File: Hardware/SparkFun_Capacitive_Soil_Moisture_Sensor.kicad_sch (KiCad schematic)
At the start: 21 parts, among them J1 Qwiic_RA, J2 Qwiic_RA, U1 CAP1203

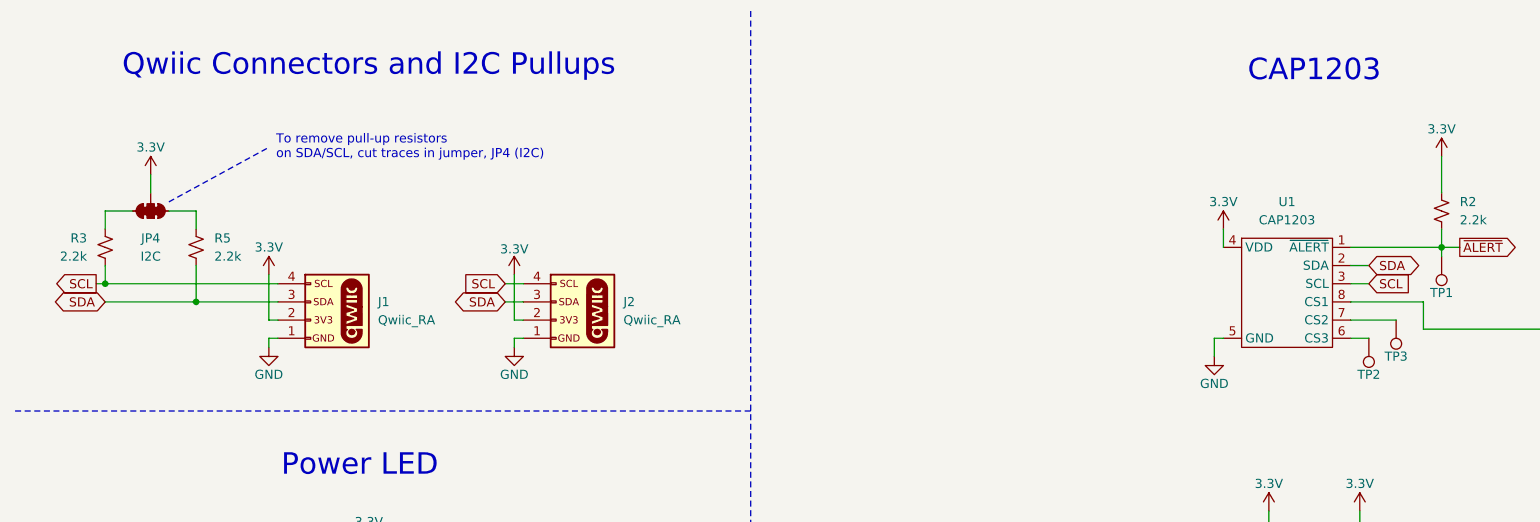
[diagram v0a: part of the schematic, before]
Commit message: Cleanup test points and silkscreen, remove acid traps
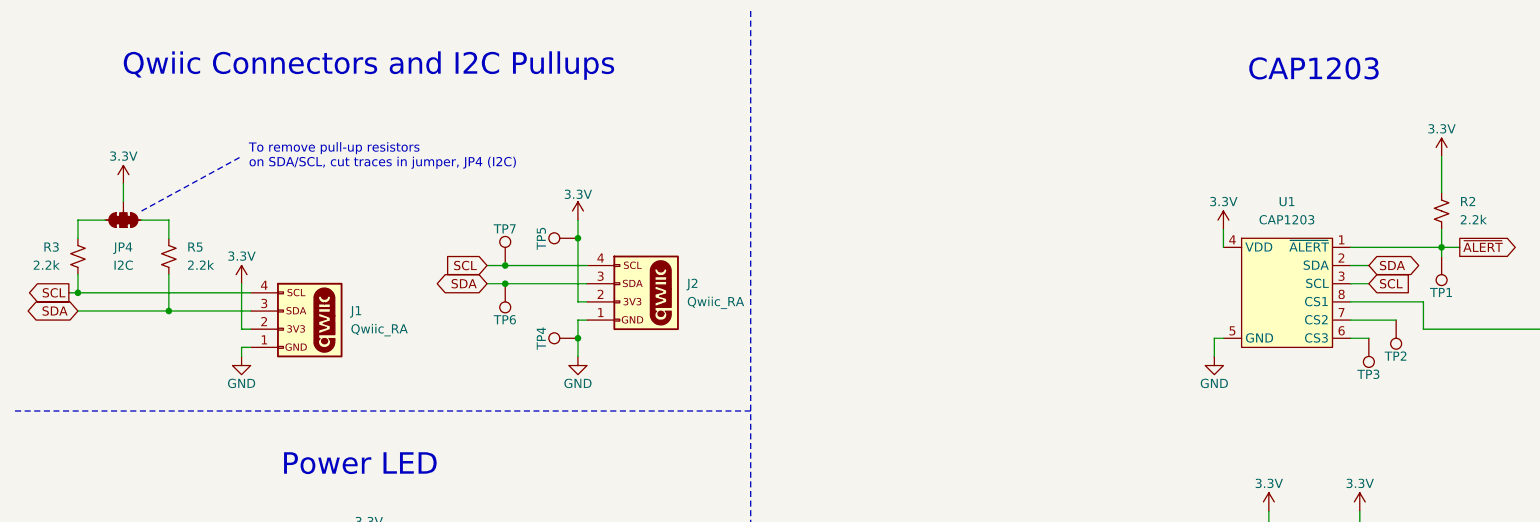
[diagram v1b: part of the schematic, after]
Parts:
- removed TP1, TP2, TP3: 1.25mm, SparkFun-Connector:TestPoint-1.25mm, symbol SparkFun-Connector:TestPoint_1.25mm
- added TP1, TP2, TP3, TP4, TP5, TP6, TP7: 1.0mm, SparkFun-Connector:TestPoint-1.0mm, symbol SparkFun-Connector:TestPoint_1.0mm
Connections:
- net 3.3V: now also TP5.1
- net GND: now also TP4.1
- net SCL: now also TP7.1
- net SDA: now also TP6.1
- net ~{ALERT}: now also TP1.1
- net at U1.7 (CS2): now also TP2.1
- net at U1.6 (CS3): now also TP3.1
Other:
- moved on the sheet: J1, J2, JP4, R3, R5

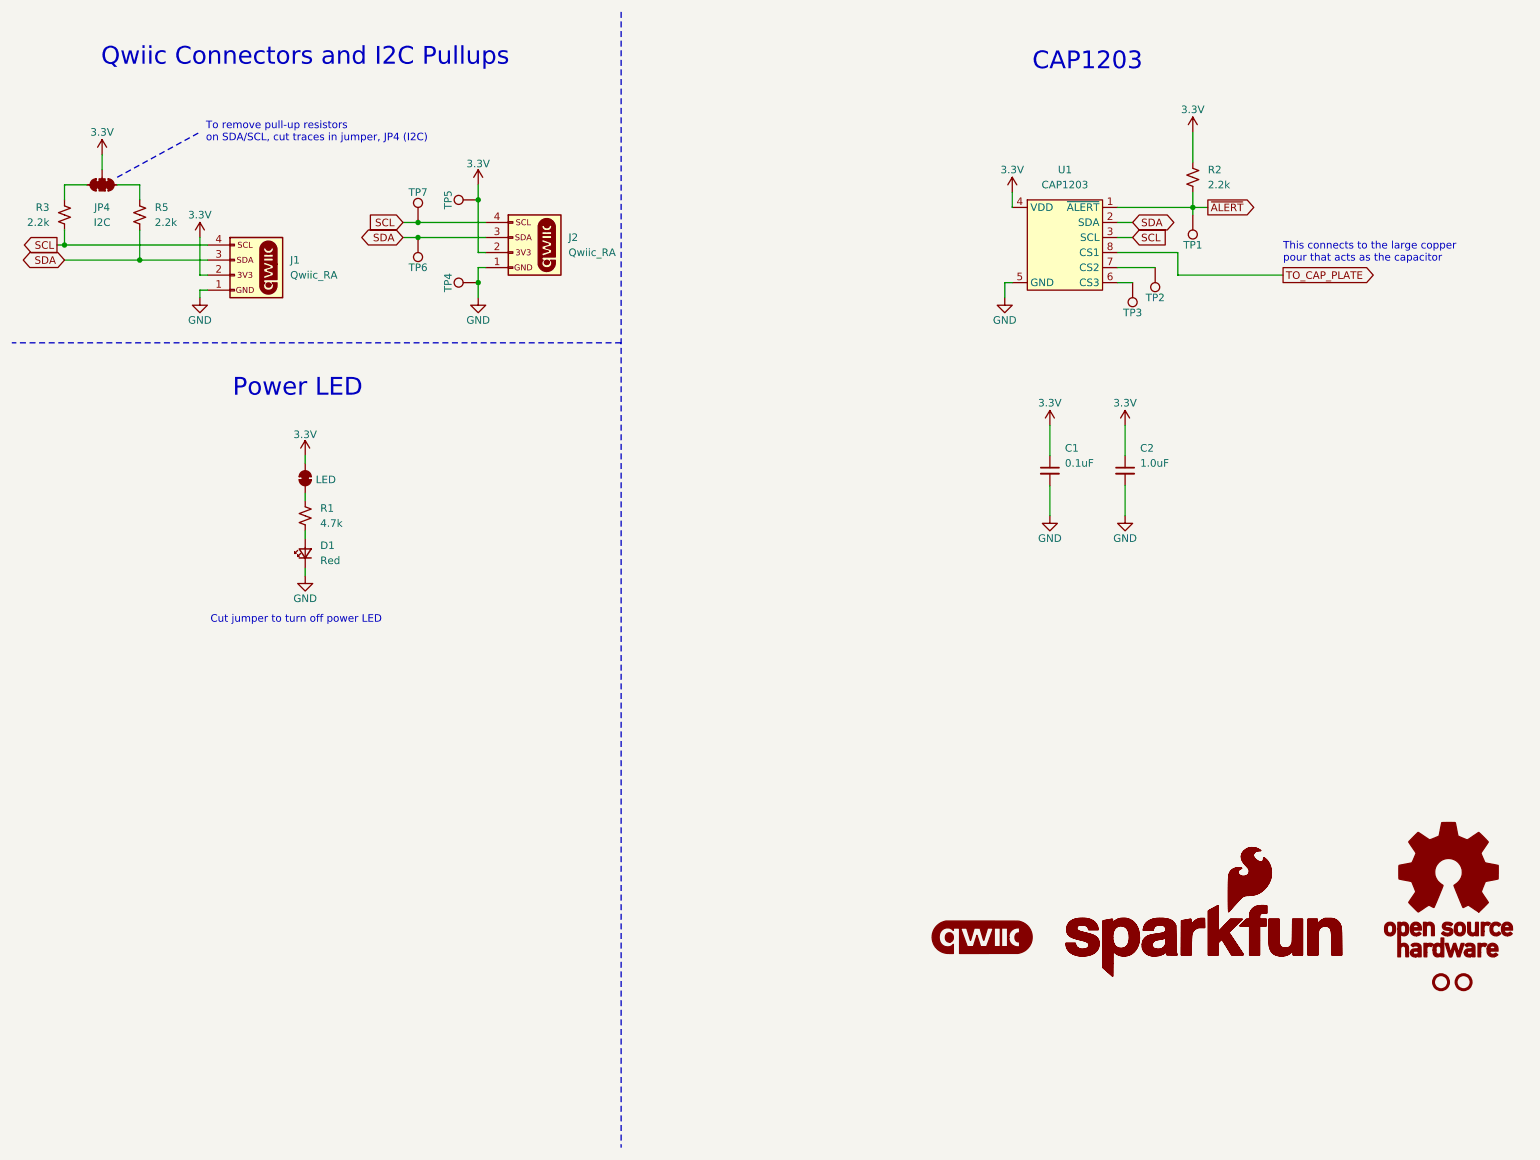
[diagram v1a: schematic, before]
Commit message: Make schematic updates from preliminary review
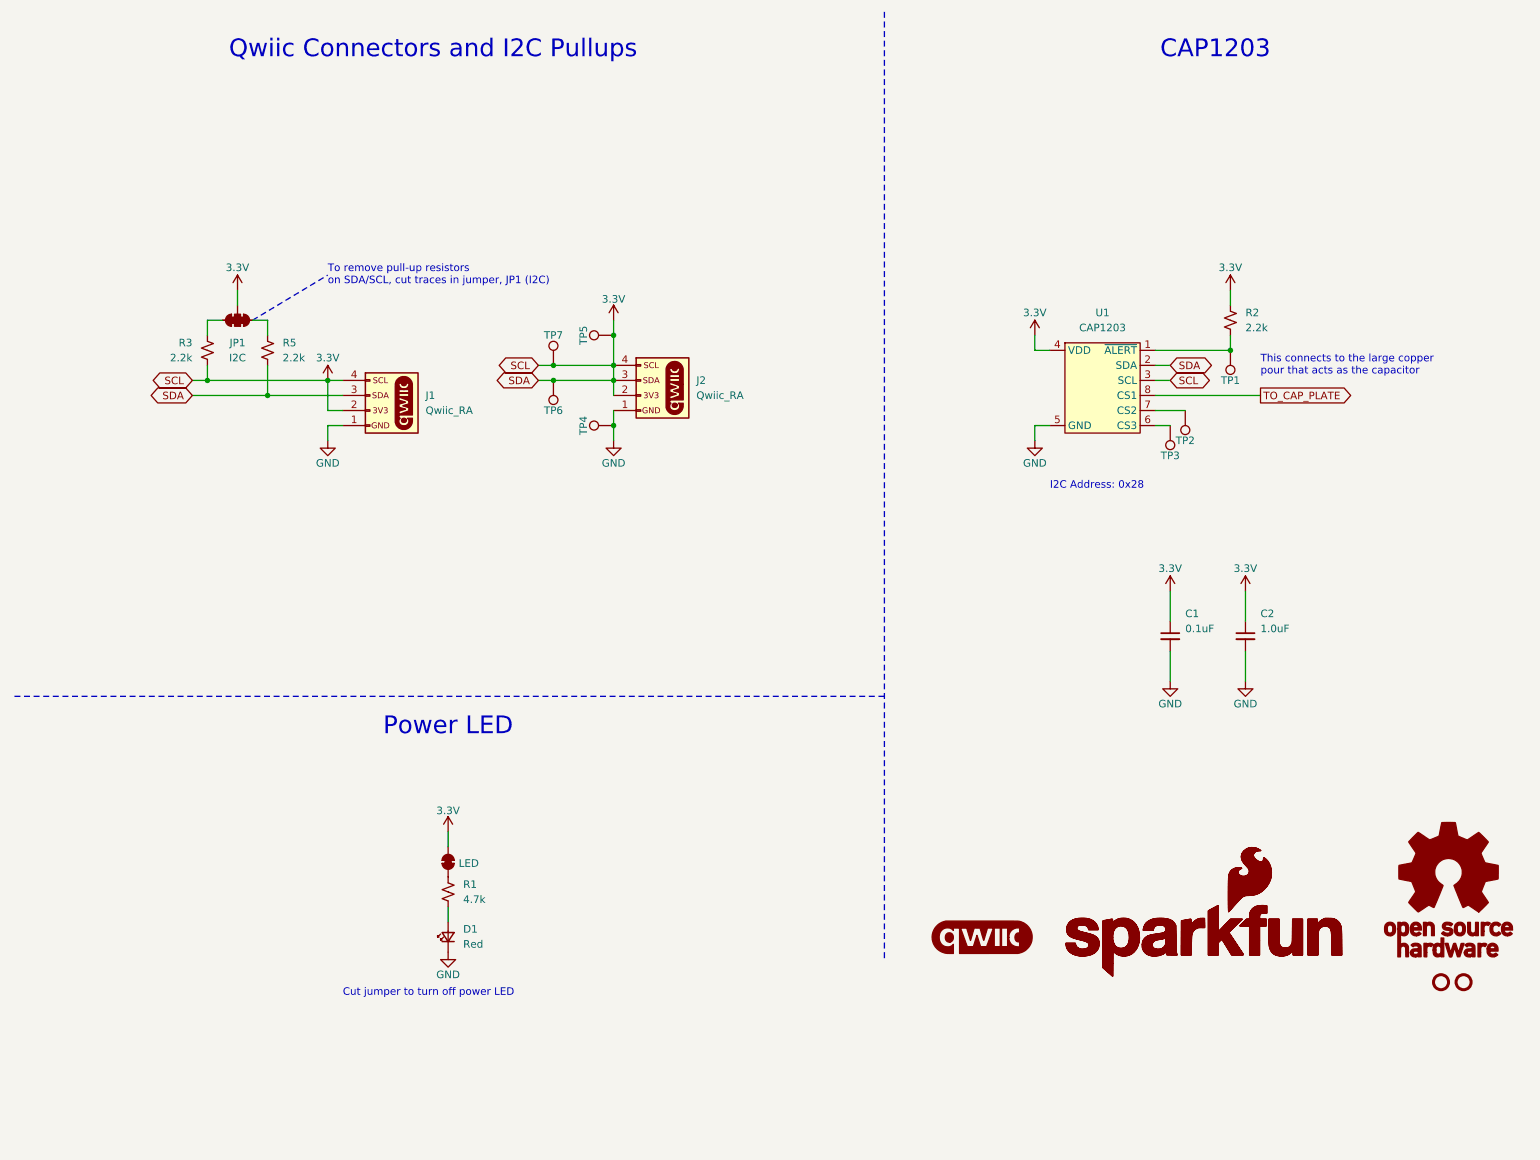
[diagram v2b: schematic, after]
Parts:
- renumbered JP4 to JP1
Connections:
- net SCL is gone; now on net 3.3V: J1.4 (Pin_4), J2.4 (Pin_4), R3.2, TP7.1, U1.3 (SCL)
- net SDA is gone; now on net 3.3V: J1.3 (Pin_3), J2.3 (Pin_3), R5.2, TP6.1, U1.2 (SDA)
- net ~{ALERT}: no longer names the net of R2.2, TP1.1, U1.1 (~{ALERT})
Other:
- note added: "I2C Address: 0x28"
- note added: "To remove pull-up resistors on SDA/SCL, cut traces in jumper, JP1 (I2C)"
- note removed: "To remove pull-up resistors on SDA/SCL, cut traces in jumper, JP4 (I2C)"
- moved on the sheet: C1, C2, D1, J1, J2, JP1, R1, R2, R3, R5, TP1, TP2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

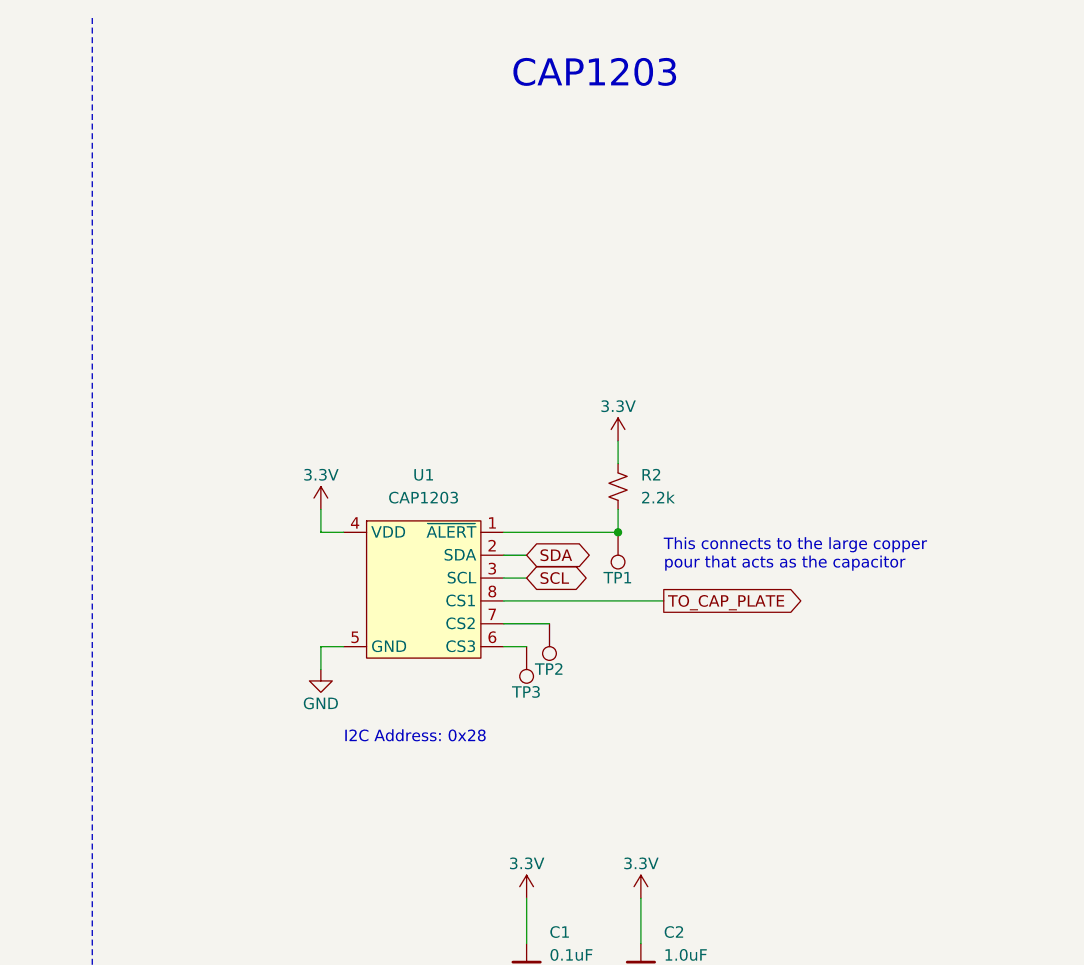
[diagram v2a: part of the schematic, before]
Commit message: Update schematic with new cap sensing chip
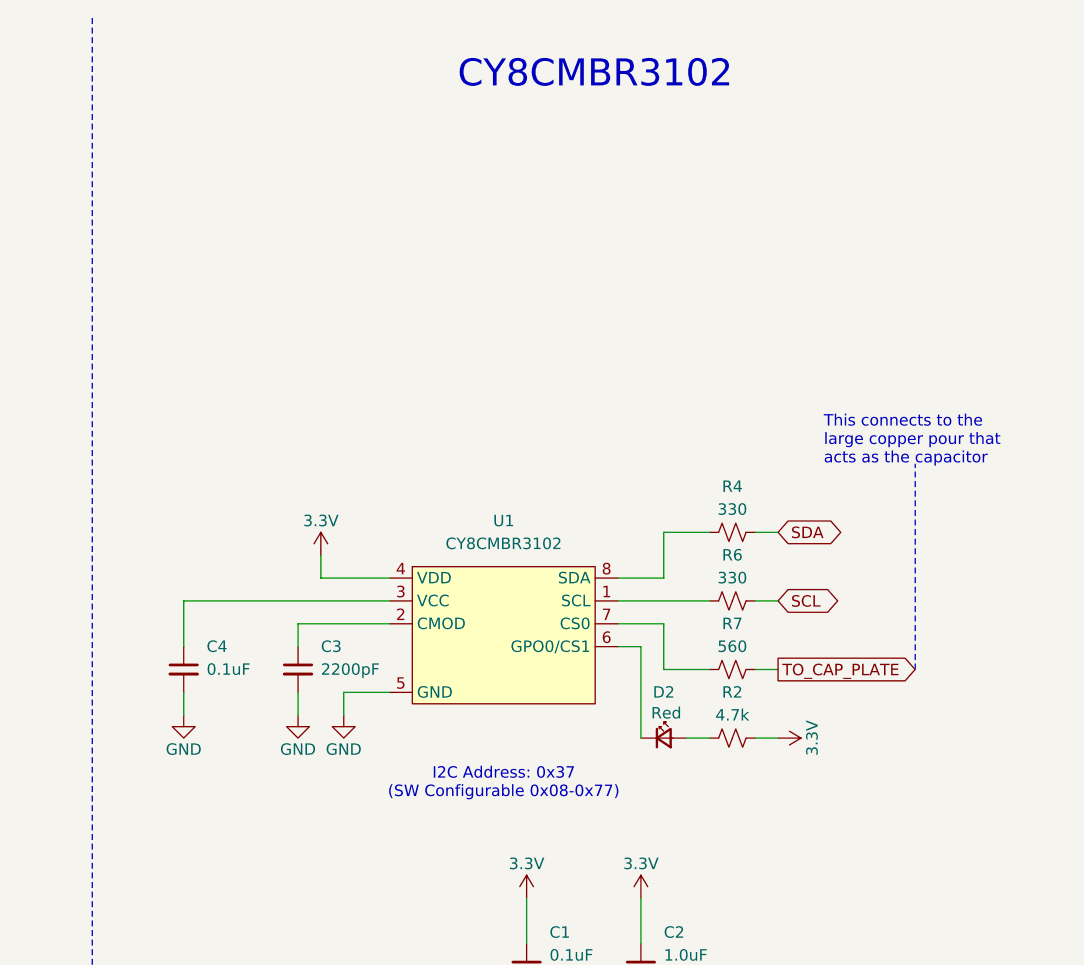
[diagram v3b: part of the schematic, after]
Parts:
- removed R2: 2.2k, SparkFun-Resistor:R_0603_1608Metric, symbol SparkFun-Resistor:2.2k_0603
- removed TP1, TP2, TP3: 1.0mm, SparkFun-Connector:TestPoint-1.0mm, symbol SparkFun-Connector:TestPoint_1.0mm
- removed U1: CAP1203, SparkFun-Semiconductor-Standard:SO-8, symbol SparkFun-Sensor:CAP1203
- added C3: 2200pF, SparkFun-Capacitor:C_0402_1005Metric, symbol SparkFun-Capacitor:2200pF_0402_50V_10%
- added C4: 0.1uF, SparkFun-Capacitor:C_0603_1608Metric, symbol SparkFun-Capacitor:0.1uF_0603_25V_20%
- added D2: Red, SparkFun-LED:LED_0603_1608Metric_Red, symbol SparkFun-LED:LED_Red_0603
- added R2: 4.7k, SparkFun-Resistor:R_0603_1608Metric, symbol SparkFun-Resistor:4.7k_0603
- added R4, R6: 330, SparkFun-Resistor:R_0603_1608Metric, symbol SparkFun-Resistor:330_0603
- added R7: 560, SparkFun-Resistor:R_0402_1005Metric, symbol SparkFun-Resistor:560_0402
- added U1: CY8CMBR3102, SparkFun-Semiconductor-Standard:SO-8, symbol SparkFun-Sensor:CY8CMBR3102
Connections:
- net 3.3V: now also R2.1, R4.2, R6.2, U1.4 (VDD)
- net GND: now also C3.2, C4.2, U1.5 (GND)
- net TO_CAP_PLATE: now also R7.2
- new net: R6.1, U1.1 (SCL)
- new net: C3.1, U1.2 (CMOD)
- new net: C4.1, U1.3 (VCC)
- new net: D2.1 (K), U1.6 (GPO0/CS1)
- new net: R7.1, U1.7 (CS0)
- new net: R4.1, U1.8 (SDA)
- new net: D2.2 (A), R2.2
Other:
- note added: "CY8CMBR3102"
- note added: "I2C Address: 0x37 (SW Configurable 0x08-0x77)"
- note removed: "CAP1203"
- note removed: "I2C Address: 0x28"

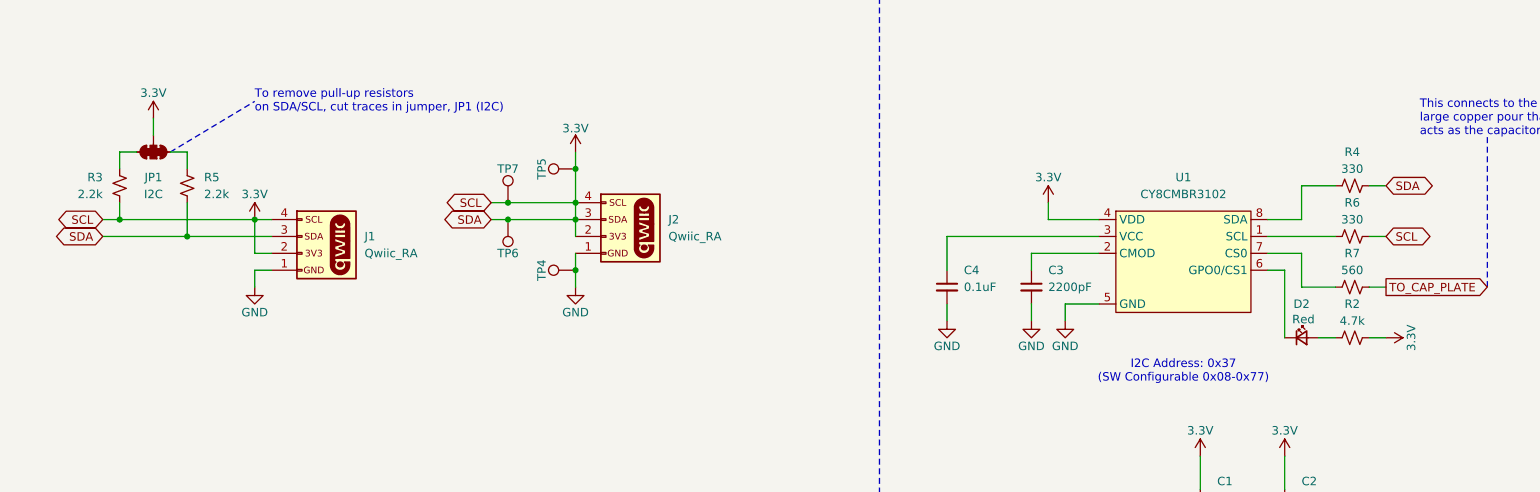
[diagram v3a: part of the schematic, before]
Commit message: Add schematic fixes from initial review
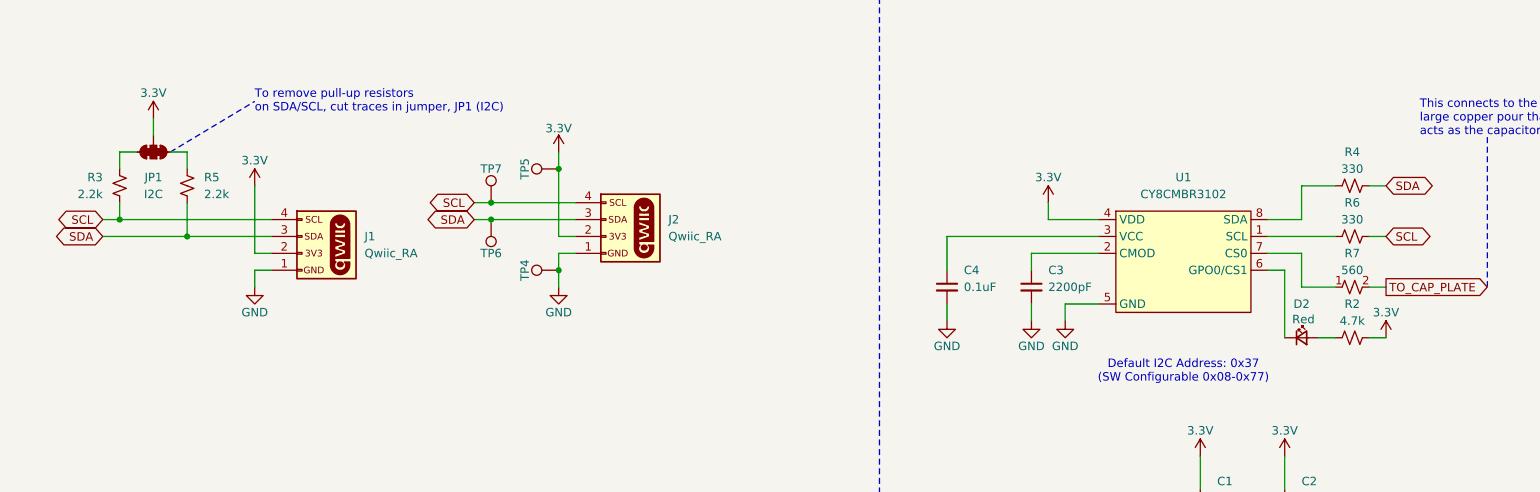
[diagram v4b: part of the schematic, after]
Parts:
- R7: footprint SparkFun-Resistor:R_0402_1005Metric -> SparkFun-Resistor:R_0603_1608Metric; symbol SparkFun-Resistor:560_0402 -> SparkFun-Resistor:560_0603; PROD_ID RES-13766 -> TODO:PROD_ID
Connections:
- net 3.3V: no longer J1.3 (Pin_3), J1.4 (Pin_4), J2.3 (Pin_3), J2.4 (Pin_4), R3.2, R4.2, R5.2, R6.2, TP6.1, TP7.1
- new net SCL: J1.4 (Pin_4), J2.4 (Pin_4), R3.2, R6.2, TP7.1
- new net SDA: J1.3 (Pin_3), J2.3 (Pin_3), R4.2, R5.2, TP6.1
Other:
- note added: "Default I2C Address: 0x37 (SW Configurable 0x08-0x77)"
- note removed: "I2C Address: 0x37 (SW Configurable 0x08-0x77)"
- moved on the sheet: TP4, TP5, TP6, TP7
